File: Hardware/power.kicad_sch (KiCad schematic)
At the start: 67 parts, among them J4 Barrel_Jack_Switch, U1 STM32MP157FAD1, U4 STPMIC1

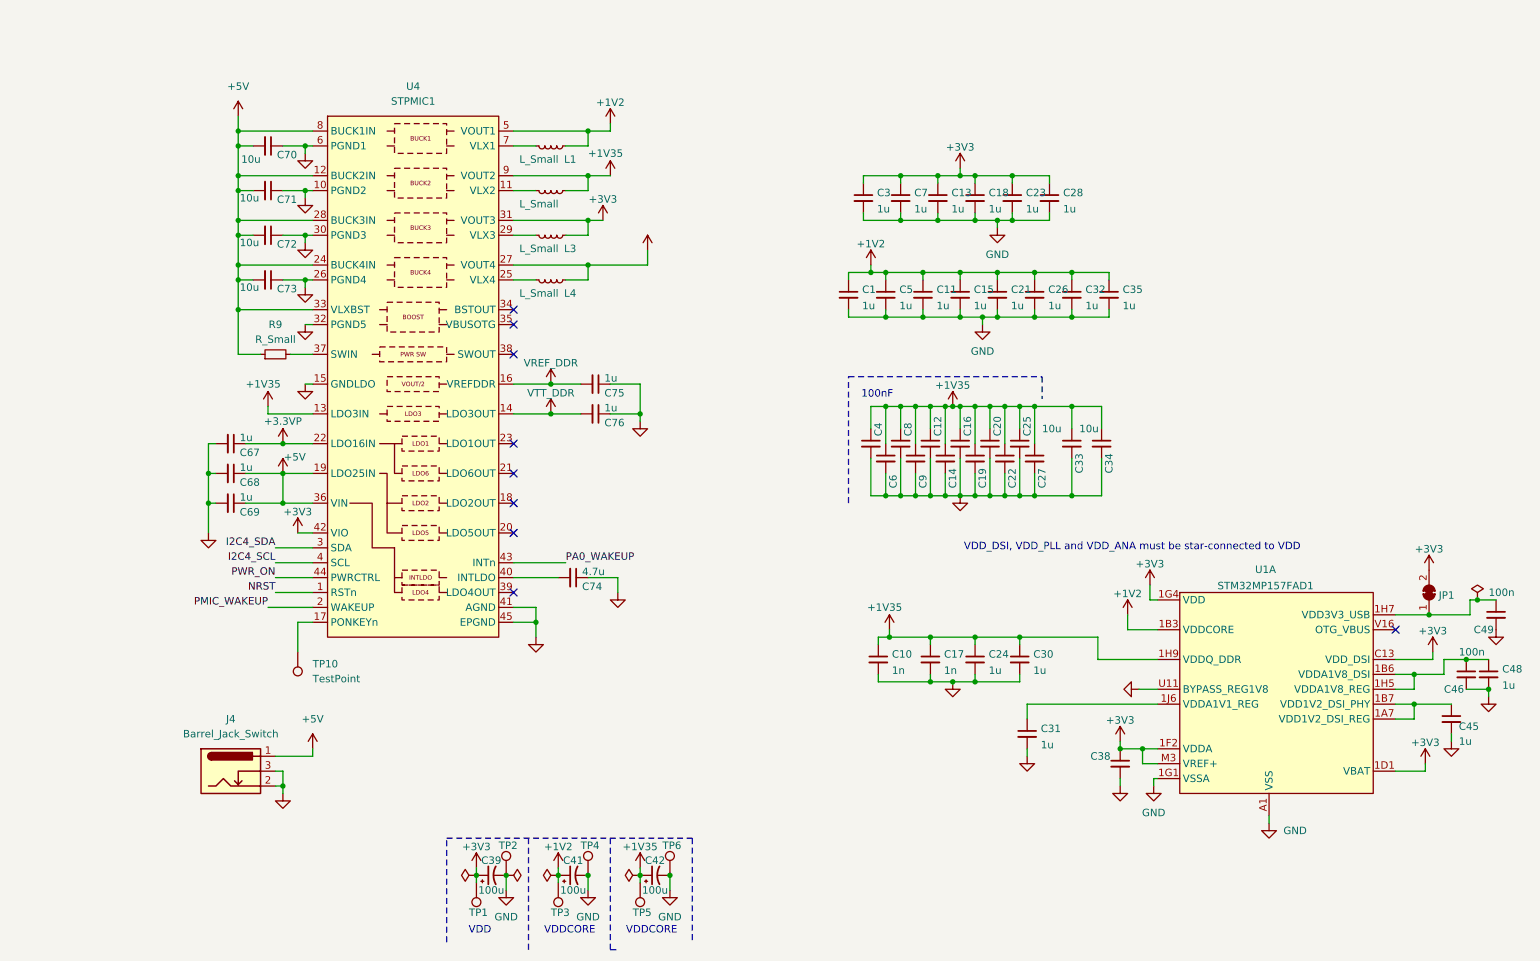
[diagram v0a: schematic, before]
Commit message: Create libraries and move custom symbols to project specific libraries
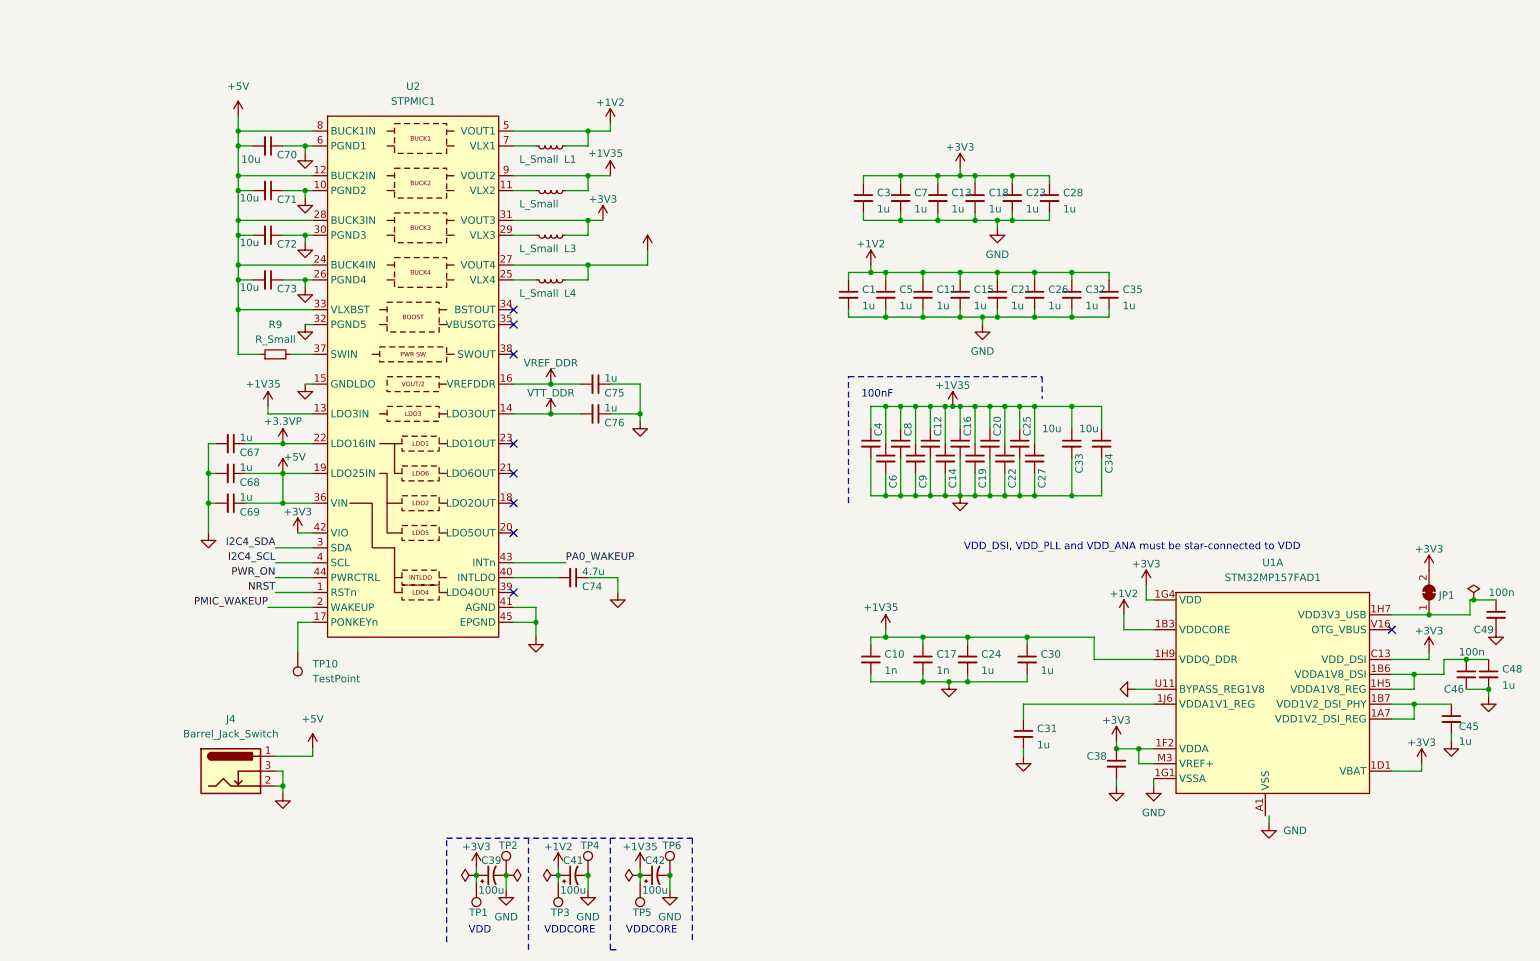
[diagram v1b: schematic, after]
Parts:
- removed U1: STM32MP157FAD1, personal:TFBGA257, symbol Personal:STM32MP157FAD1
- removed U4: STPMIC1, BioMEMS:WFQFN44L, symbol BioMEMS:STPMIC1APQR
- added U1: STM32MP157FAD1, personal:TFBGA257, symbol SimpleSBC:STM32MP157FAD1
- added U2: STPMIC1, BioMEMS:WFQFN44L, symbol SimpleSBC:STPMIC1APQR
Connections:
- net +1V2: now also U1.1B3 (VDDCORE), U1.1B5 (VDDCORE), U1.1C4 (VDDCORE), U1.1C6 (VDDCORE), U1.1D3 (VDDCORE), U1.1D5 (VDDCORE), U1.1D7 (VDDCORE), U1.1E4 (VDDCORE), U1.1E6 (VDDCORE), U1.1E8 (VDDCORE), U1.1F5 (VDDCORE), U1.1F7 (VDDCORE), U1.1G6 (VDDCORE), U1.1G8 (VDDCORE), U2.5 (VOUT1)
- net +1V35: now also U1.1B9 (VDDQ_DDR), U1.1D9 (VDDQ_DDR), U1.1F9 (VDDQ_DDR), U1.1H9 (VDDQ_DDR), U2.13 (LDO3IN), U2.9 (VOUT2)
- net +3.3VP: now also U2.22 (LDO16IN), U2.27 (VOUT4)
- net +3V3: now also U1.1D1 (VBAT), U1.1E2 (VDD), U1.1F1 (VDDA), U1.1F2 (VDDA), U1.1F3 (VDD), U1.1G3 (VDD), U1.1G4 (VDD), U1.1J3 (VDD), U1.C13 (VDD_DSI), U1.M3 (VREF+), U2.31 (VOUT3), U2.42 (VIO)
- net +5V: now also U2.12 (BUCK2IN), U2.19 (LDO25IN), U2.24 (BUCK4IN), U2.28 (BUCK3IN), U2.33 (VLXBST), U2.36 (VIN), U2.8 (BUCK1IN)
- net GND: now also U1.1G1 (VSSA), U1.U11 (BYPASS_REG1V8), U2.10 (PGND2), U2.15 (GNDLDO), U2.26 (PGND4), U2.30 (PGND3), U2.32 (PGND5), U2.41 (AGND), U2.45 (EPGND), U2.6 (PGND1)
- net I2C4_SCL: now also U2.4 (SCL)
- net I2C4_SDA: now also U2.3 (SDA)
- net NRST: now also U2.1 (RSTn)
- net PA0_WAKEUP: now also U2.43 (INTn)
- net PMIC_WAKEUP: now also U2.2 (WAKEUP)
- net PWR_ON: now also U2.44 (PWRCTRL)
- net VREF_DDR: now also U2.16 (VREFDDR)
- net VTT_DDR: now also U2.14 (LDO3OUT)
- net at L2.1: now also U2.11 (VLX2)
- net at C49.1, JP1.1 (A): now also U1.1H7 (VDD3V3_USB)
- net at R9.2: now also U2.37 (SWIN)
- net at C46.1, C48.1: now also U1.1B6 (VDDA1V8_DSI), U1.1H5 (VDDA1V8_REG)
- net at C45.1: now also U1.1A7 (VDD1V2_DSI_REG), U1.1B7 (VDD1V2_DSI_PHY)
- net at C74.2: now also U2.40 (INTLDO)
- net at C31.1: now also U1.1J6 (VDDA1V1_REG)
- net at TP10.1: now also U2.17 (PONKEYn)
- net at L3.1: now also U2.29 (VLX3)
- net at L4.1: now also U2.25 (VLX4)
- net at L1.1: now also U2.7 (VLX1)
- new net VSS: U1.1A6 (VSS), U1.1B8 (VSS), U1.1C3 (VSS), U1.1C5 (VSS), U1.1C7 (VSS), U1.1D2 (VSS), U1.1D4 (VSS), U1.1D6 (VSS), U1.1E3 (VSS), U1.1E5 (VSS), U1.1E7 (VSS), U1.1F4 (VSS), U1.1F6 (VSS), U1.1G2 (VSS), U1.1G5 (VSS), U1.1G7 (VSS), U1.1H2 (VSS), U1.1H3 (VSS), U1.1H4 (VSS), U1.1H6 (VSS), U1.1H8 (VSS), U1.1J5 (VSS), U1.1J9 (VSS), U1.A1 (VSS), U1.A19 (VSS), U1.A6 (VSS), U1.C14 (VSS), U1.D17 (VSS), U1.F18 (VSS), U1.F3 (VSS), U1.G1 (VSS), U1.G17 (VSS), U1.K17 (VSS), U1.K19 (VSS), U1.N1 (VSS), U1.N17 (VSS), U1.R19 (VSS), U1.U9 (VSS), U1.W1 (VSS), U1.W13 (VSS), U1.W19 (VSS), U1.W5 (VSS)
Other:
- moved on the sheet: C10, C17, C24, C30, C31, C38

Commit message: First Draft schematic (R2)
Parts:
- removed C39, C41, C42: 100u, Capacitor_SMD:C_1206_3216Metric, symbol Device:C_Polarized_Small_US
- removed U2: STPMIC1, BioMEMS:WFQFN44L, symbol SimpleSBC:STPMIC1APQR
- added U4: STPMIC1, SimpleSBC:WFQFN44L, symbol SimpleSBC:STPMIC1APQR
- TP1, TP2, TP3, TP4, TP5, TP6: value TestPoint-SP -> TestPoint; footprint personal:PROBE_PAD_1206 -> (none)
- U1: footprint personal:TFBGA257 -> SimpleSBC:TFBGA257
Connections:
- net VSS is gone; now on net GND: U1.1A6 (VSS), U1.1B8 (VSS), U1.1C3 (VSS), U1.1C5 (VSS), U1.1C7 (VSS), U1.1D2 (VSS), U1.1D4 (VSS), U1.1D6 (VSS), U1.1E3 (VSS), U1.1E5 (VSS), U1.1E7 (VSS), U1.1F4 (VSS), U1.1F6 (VSS), U1.1G2 (VSS), U1.1G5 (VSS), U1.1G7 (VSS), U1.1H2 (VSS), U1.1H3 (VSS), U1.1H4 (VSS), U1.1H6 (VSS), U1.1H8 (VSS), U1.1J5 (VSS), U1.1J9 (VSS), U1.A1 (VSS), U1.A19 (VSS), U1.A6 (VSS), U1.C14 (VSS), U1.D17 (VSS), U1.F18 (VSS), U1.F3 (VSS), U1.G1 (VSS), U1.G17 (VSS), U1.K17 (VSS), U1.K19 (VSS), U1.N1 (VSS), U1.N17 (VSS), U1.R19 (VSS), U1.U9 (VSS), U1.W1 (VSS), U1.W13 (VSS), U1.W19 (VSS), U1.W5 (VSS)
- net +1V2: now also TP1.1, U4.5 (VOUT1); no longer TP3.1
- net +1V35: now also TP2.1, U4.13 (LDO3IN), U4.9 (VOUT2); no longer TP5.1
- net +3.3VP: now also TP4.1, U4.22 (LDO16IN), U4.27 (VOUT4)
- net +3V3: now also TP3.1, U4.31 (VOUT3), U4.42 (VIO); no longer TP1.1
- net +5V: now also U4.12 (BUCK2IN), U4.19 (LDO25IN), U4.24 (BUCK4IN), U4.28 (BUCK3IN), U4.33 (VLXBST), U4.36 (VIN), U4.8 (BUCK1IN)
- net GND: now also U4.10 (PGND2), U4.15 (GNDLDO), U4.26 (PGND4), U4.30 (PGND3), U4.32 (PGND5), U4.41 (AGND), U4.45 (EPGND), U4.6 (PGND1); no longer TP2.1, TP4.1, TP6.1
- net I2C4_SCL: now also U4.4 (SCL)
- net I2C4_SDA: now also U4.3 (SDA)
- net NRST: now also U4.1 (RSTn)
- net PA0_WAKEUP: now also U4.43 (INTn)
- net PMIC_WAKEUP: now also U4.2 (WAKEUP)
- net PWR_ON: now also U4.44 (PWRCTRL)
- net VREF_DDR: now also TP5.1, U4.16 (VREFDDR)
- net VTT_DDR: now also TP6.1, U4.14 (LDO3OUT)
- net at L2.1: now also U4.11 (VLX2)
- net at R9.2: now also U4.37 (SWIN)
- net at C74.2: now also U4.40 (INTLDO)
- net at TP10.1: now also U4.17 (PONKEYn)
- net at L3.1: now also U4.29 (VLX3)
- net at L4.1: now also U4.25 (VLX4)
- net at L1.1: now also U4.7 (VLX1)
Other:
- note removed: "VDD"
- note removed: "VDDCORE"
- title: (none) -> SimpleSBC Power
- moved on the sheet: C1, C10, C11, C12, C13, C14, C15, C16, C17, C18, C19, C20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

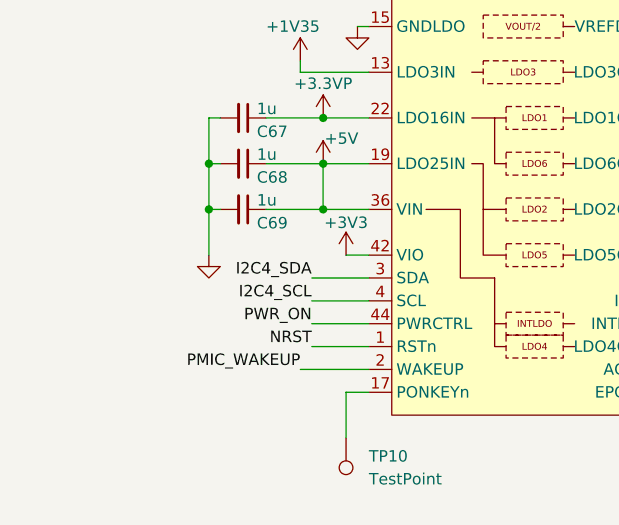
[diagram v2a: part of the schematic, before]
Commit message: Add Ethernet and USB power switching
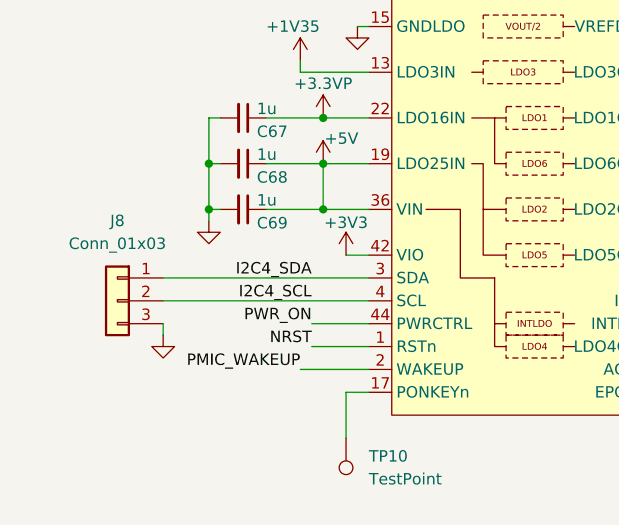
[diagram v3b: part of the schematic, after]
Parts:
- added J8: Conn_01x03, symbol Connector_Generic:Conn_01x03
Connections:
- net GND: now also J8.3 (Pin_3)
- net I2C4_SCL: now also J8.2 (Pin_2)
- net I2C4_SDA: now also J8.1 (Pin_1)
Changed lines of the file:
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@@
 		(date "2025-02-03")
 		(rev "2")
-		(comment 1 "Designed by Hans Gaensbauer")
+		(comment 1 "Hans Gaensbauer and Tim Shepard")
 	)
 	(junction
@@
 	(wire
 		(pts
+			(xy 34.29 138.43) (xy 57.15 138.43)
+		)
+		(stroke
+			(width 0)
+			(type default)
+		)
+	)
+	(wire
+		(pts
 			(xy 38.1 29.21) (xy 38.1 31.75)
 		)
@@
 	(wire
 		(pts
-			(xy 39.37 135.89) (xy 39.37 130.81)
+			(xy 39.37 132.08) (xy 39.37 130.81)
 		)
 		(stroke
@@
 	(wire
 		(pts
+			(xy 34.29 140.97) (xy 57.15 140.97)
+		)
+		(stroke
+			(width 0)
+			(type default)
+		)
+	)
+	(wire
+		(pts
 			(xy 172.72 36.83) (xy 172.72 35.56)
 		)
@@
 	(wire
 		(pts
-			(xy 50.8 138.43) (xy 57.15 138.43)
+			(xy 186.69 74.93) (xy 187.96 74.93)
 		)
 		(stroke
@@
 	(wire
 		(pts
-			(xy 186.69 74.93) (xy 187.96 74.93)
+			(xy 34.29 143.51) (xy 34.29 144.78)
 		)
 		(stroke
@@
 	(wire
 		(pts
-			(xy 50.8 140.97) (xy 57.15 140.97)
-		)
-		(stroke
-			(width 0)
-			(type default)
-		)
-	)
-	(wire
-		(pts
 			(xy 189.23 74.93) (xy 191.77 74.93)
 		)
@@
 	(symbol
 		(lib_id "power:GND")
-		(at 39.37 135.89 0)
+		(at 39.37 132.08 0)
 		(unit 1)
 		(exclude_from_sim no)
@@
 		(fields_autoplaced yes)
 		(property "Reference" "#PWR015"
-			(at 39.37 142.24 0)
+			(at 39.37 138.43 0)
 			(effects
 				(font
@@
 		)
 		(property "Value" "GND"
-			(at 39.849 135.255 90)
+			(at 39.849 131.445 90)
 			(effects
 				(font
@@
 		)
 		(property "Footprint" ""
-			(at 39.37 135.89 0)
+			(at 39.37 132.08 0)
 			(effects
 				(font
@@
 		)
 		(property "Datasheet" ""
-			(at 39.37 135.89 0)
+			(at 39.37 132.08 0)
 			(effects
 				(font
@@
 		)
 		(property "Description" ""
-			(at 39.37 135.89 0)
+			(at 39.37 132.08 0)
 			(effects
 				(font
@@
 	)
 	(symbol
+		(lib_id "Connector_Generic:Conn_01x03")
+		(at 29.21 140.97 0)
+		(mirror y)
+		(unit 1)
+		(exclude_from_sim no)
+		(in_bom yes)
+		(on_board yes)
+		(dnp no)
+		(fields_autoplaced yes)
+		(property "Reference" "J8"
+			(at 29.21 132.08 0)
+			(effects
+				(font
+					(size 1.27 1.27)
+				)
+			)
+		)
+		(property "Value" "Conn_01x03"
+			(at 29.21 134.62 0)
+			(effects
+				(font
+					(size 1.27 1.27)
+				)
+			)
+		)
+		(property "Footprint" ""
+			(at 29.21 140.97 0)
+			(effects
+				(font
+					(size 1.27 1.27)
+				)
+				(hide yes)
+			)
+		)
+		(property "Datasheet" "~"
+			(at 29.21 140.97 0)
+			(effects
+				(font
+					(size 1.27 1.27)
+				)
+				(hide yes)
+			)
+		)
+		(property "Description" "Generic connector, single row, 01x03, script generated (kicad-library-utils/schlib/autogen/connector/)"
+			(at 29.21 140.97 0)
+			(effects
+				(font
+					(size 1.27 1.27)
+				)
+				(hide yes)
+			)
+		)
+		(pin "2"
+		)
+		(pin "1"
+		)
+		(pin "3"
+		)
+		(instances
+			(project ""
+				(path "/78ab8a62-95bb-407d-9a77-e3716c9faf5c/64c924ff-1ee2-4076-8d5b-d4197d44b396"
+					(reference "J8")
+					(unit 1)
+				)
+			)
+		)
+	)
+	(symbol
 		(lib_id "Connector:TestPoint")
 		(at 105.41 105.41 270)
@@
 					(unit 1)
 				)
+			)
+		)
+	)
+	(symbol
+		(lib_id "power:GND")
+		(at 34.29 144.78 0)
+		(unit 1)
+		(exclude_from_sim no)
+		(in_bom yes)
+		(on_board yes)
+		(dnp no)
+		(fields_autoplaced yes)
+		(property "Reference" "#PWR0107"
+			(at 34.29 151.13 0)
+			(effects
+				(font
+					(size 1.27 1.27)
+				)
+				(hide yes)
+			)
+		)
+		(property "Value" "GND"
+			(at 34.769 144.145 90)
+			(effects
+				(font
+					(size 1.27 1.27)
+				)
+				(justify left)
+				(hide yes)
+			)
+		)
+		(property "Footprint" ""
+			(at 34.29 144.78 0)
+			(effects
+				(font
+					(size 1.27 1.27)
+				)
+				(hide yes)
+			)
+		)
+		(property "Datasheet" ""
+			(at 34.29 144.78 0)
+			(effects
+				(font
+					(size 1.27 1.27)
+				)
+				(hide yes)
+			)
+		)
+		(property "Description" ""
+			(at 34.29 144.78 0)
+			(effects
+				(font
+					(size 1.27 1.27)
+				)
+				(hide yes)
+			)
+		)
+		(pin "1"
+		)
+		(instances
+			(project "simpleSBC"
+				(path "/78ab8a62-95bb-407d-9a77-e3716c9faf5c/64c924ff-1ee2-4076-8d5b-d4197d44b396"
+					(reference "#PWR0107")
+					(unit 1)
+				)
